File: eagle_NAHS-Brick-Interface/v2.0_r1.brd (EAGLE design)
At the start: 21.5 x 40 mm, 11 parts, among them IC1 FT232RL, J1 NAHS-BRICK-INTERFACE-V2_I-SIDE, J2 10118194-0001LF

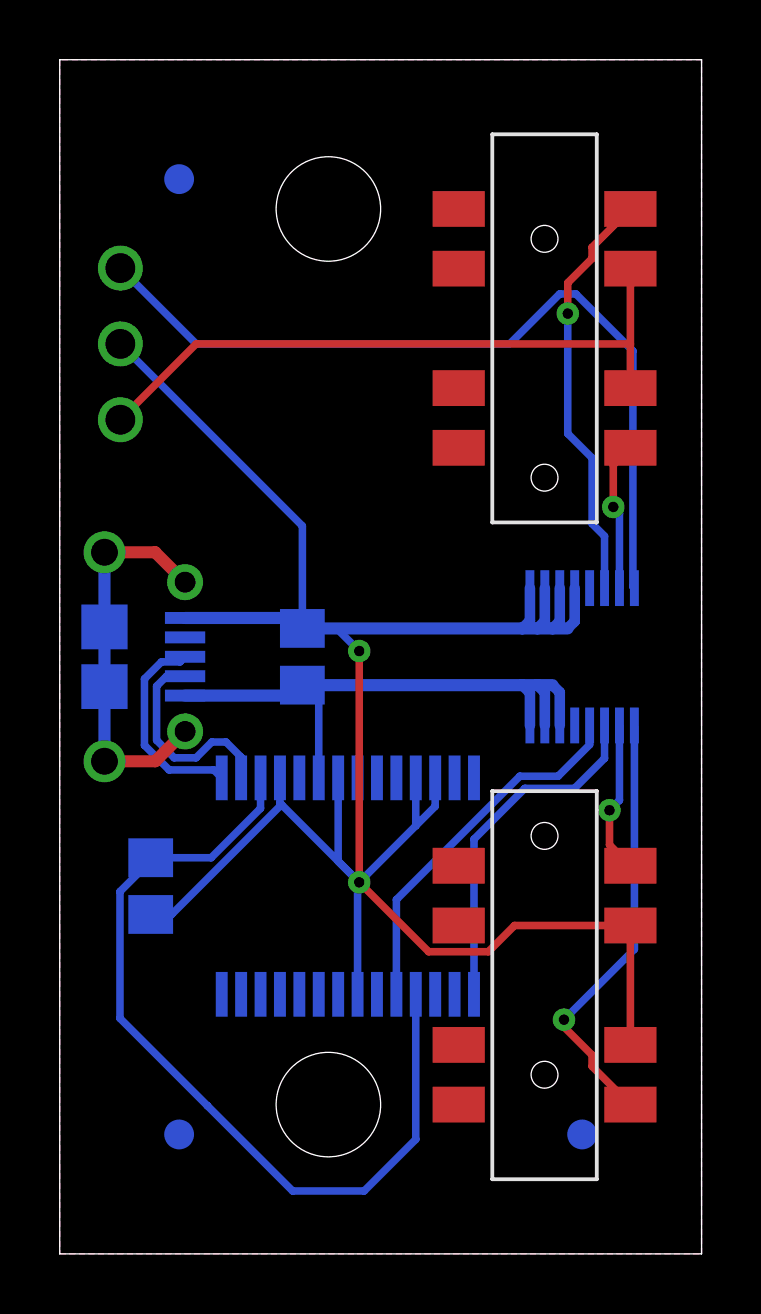
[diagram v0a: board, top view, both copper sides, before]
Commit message: added third UPDI Pin
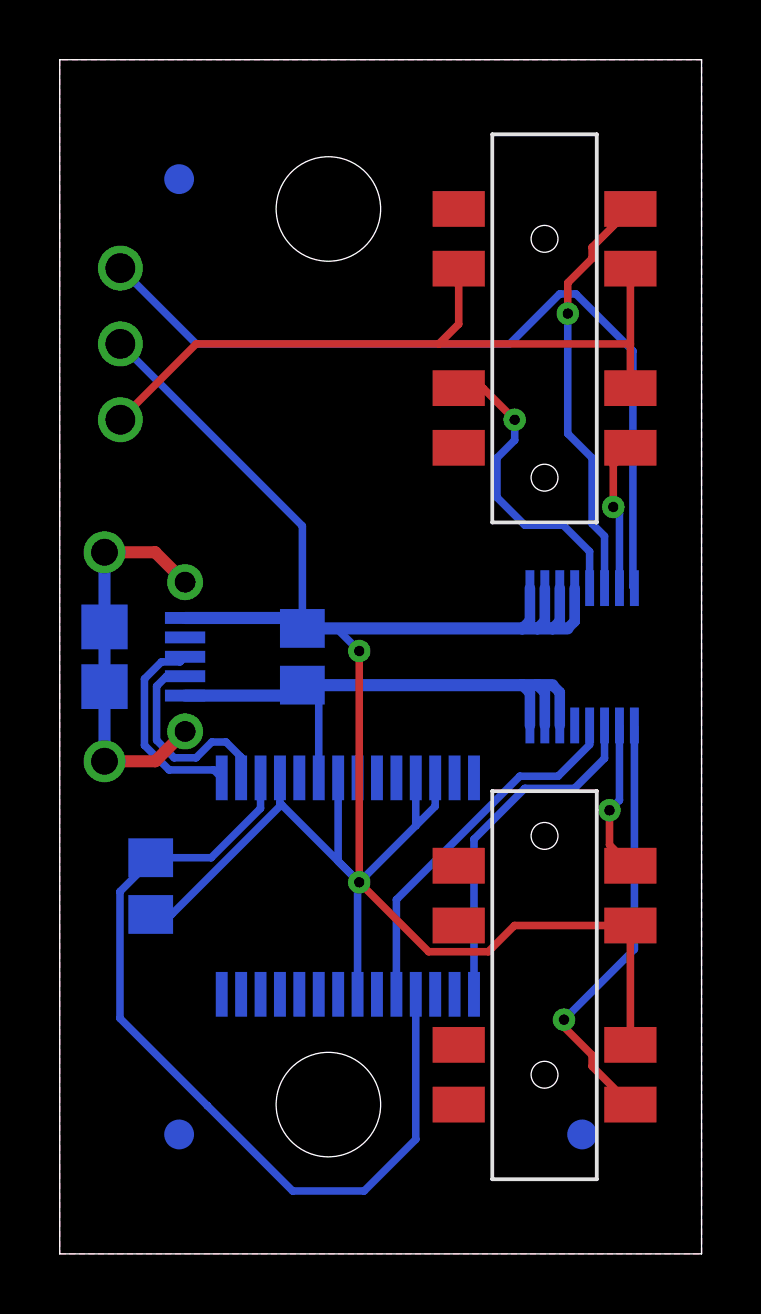
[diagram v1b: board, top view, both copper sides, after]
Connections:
- new net UPDI3: J1.12, S1.1.3
- net UPDI: now also S1.1.2
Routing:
- net UPDI3: track 0.00 -> 10.2 mm, vias 0 -> 1
- net UPDI: track 22.1 -> 24.9 mm
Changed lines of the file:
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@@
 <setting verticaltext="up"/>
 </settings>
-<grid distance="100" unitdist="mil" unit="mm" style="lines" multiple="1" display="no" altdistance="5" altunitdist="mil" altunit="mil"/>
+<grid distance="100" unitdist="mil" unit="mil" style="lines" multiple="1" display="no" altdistance="5" altunitdist="mil" altunit="mil"/>
 <layers>
 <layer number="1" name="Top" color="4" fill="1" visible="yes" active="yes"/>
@@
 <wire x1="19.115" y1="30.48" x2="19.115" y2="29" width="0.254" layer="1"/>
 <wire x1="2.032" y1="27.94" x2="4.572" y2="30.48" width="0.254" layer="1"/>
-<wire x1="4.572" y1="30.48" x2="19.115" y2="30.48" width="0.254" layer="1"/>
+<wire x1="4.572" y1="30.48" x2="12.7" y2="30.48" width="0.254" layer="1"/>
+<contactref element="S1" pad="1.2"/>
+<wire x1="12.7" y1="30.48" x2="19.115" y2="30.48" width="0.254" layer="1"/>
+<wire x1="13.365" y1="33" x2="13.365" y2="31.145" width="0.254" layer="1"/>
+<wire x1="13.365" y1="31.145" x2="12.7" y2="30.48" width="0.254" layer="1"/>
 </signal>
 <signal name="+3V3">
@@
 <wire x1="15.0720125" y1="30.48" x2="4.572" y2="30.48" width="0.254" layer="16"/>
 </signal>
+<signal name="UPDI3">
+<contactref element="S1" pad="1.3"/>
+<contactref element="J1" pad="12"/>
+<wire x1="17.75" y1="22.3" x2="17.75" y2="23.525" width="0.254" layer="16"/>
+<wire x1="16.868" y1="24.407" x2="15.58015625" y2="24.407" width="0.254" layer="16"/>
+<wire x1="15.58015625" y1="24.407" x2="14.647" y2="25.34015625" width="0.254" layer="16"/>
+<wire x1="14.647" y1="25.34015625" x2="14.647" y2="26.65984375" width="0.254" layer="16"/>
+<wire x1="14.647" y1="26.65984375" x2="15.24" y2="27.25284375" width="0.254" layer="16"/>
+<wire x1="15.24" y1="27.25284375" x2="15.24" y2="27.94" width="0.254" layer="16"/>
+<via x="15.24" y="27.94" extent="1-16" drill="0.35"/>
+<wire x1="15.24" y1="27.94" x2="14.18" y2="29" width="0.254" layer="1"/>
+<wire x1="14.18" y1="29" x2="13.365" y2="29" width="0.254" layer="1"/>
+<wire x1="17.75" y1="23.525" x2="16.868" y2="24.407" width="0.254" layer="16"/>
+</signal>
 </signals>
